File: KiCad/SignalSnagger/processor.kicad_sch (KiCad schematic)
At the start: 84 parts, among them J201 Conn_01x01_Female, J202 Conn_01x01_Female, J203 Conn_01x02, J204 Conn_01x02, J205 Conn_01x01_Female, J206 Conn_01x01_Female, J207 Conn_01x01_Female, J210 Conn_01x01_Female, J211 Conn_01x01_Female, J212 Conn_01x01_Female, J213 Conn_01x01_Female, J214 Conn_01x01_Female, J215 Conn_01x01_Female, J216 Conn_01x01_Female, J217 Conn_01x01_Female, J218 Conn_01x02, J219 Conn_01x02, J220 Conn_01x02, J221 Conn_01x02, P201 ISP/PDI, Q201 BSS84W-7-F, Q202 BSS138W-7-F, SW201 SW_SPST, SW202 SW_SPST, SW203 PEC12R-4225F-S0024, SW204 SW_SPST, SW205 SW_SPST, U201 AVR128DA48, U202 SI5351, U203 LP2985-5.0, U204 LP2985-3.3, U205 EA_DOGS104W-A, U206 LP2985-5.0, U207 MAX1683EUK, X202 25 MHz, X901 ECS-327TXO-30-TR

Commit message: Ver 0.317
PCB Tweaks
FreeCAD model updates
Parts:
- X901: value ECS-327TXO-30-TR -> (none); footprint Oscillator:Oscillator_SMD_ECS_327TXO -> (none)
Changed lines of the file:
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@@
   (title_block
     (title "SignalSnagger")
-    (date "2024-04-11")
-    (rev "0.316")
+    (date "2024-04-13")
+    (rev "0.317")
   )
   (bus_alias "PROC_BUS" (members "PA7" "PA6" "PA5" "PA4" "PA3" "PA2" "PA1" "PA0" "PB5" "PB4" "SCL1" "SDA1" "PB1" "PB0" "PC7" "PC6" "PC5" "PC4" "SCL0" "SDA0" "RXD1" "TXD1" "ADC7" "DAC0" "ADC5" "ADC4" "ADC3" "ADC2" "ADC1" "ADC0" "PE3" "PE2" "RXD4" "TXD4" "PF6" "PF5" "PF4" "PF3" "PF2"))
@@
     (in_bom yes) (on_board yes)
     (property "Reference" "X901" (id 0) (at 26.67 106.68 90))
-    (property "Value" "ECS-327TXO-30-TR" (id 1) (at 32.0985 105.5362 0)
+    (property "Value" "" (id 1) (at 32.0985 105.5362 0)
       (effects (font (size 1.27 1.27)) hide)
     )
-    (property "Footprint" "Oscillator:Oscillator_SMD_ECS_327TXO" (id 2) (at 52.07 114.3 0)
+    (property "Footprint" "" (id 2) (at 52.07 114.3 0)
       (effects (font (size 1.27 1.27)) hide)
     )

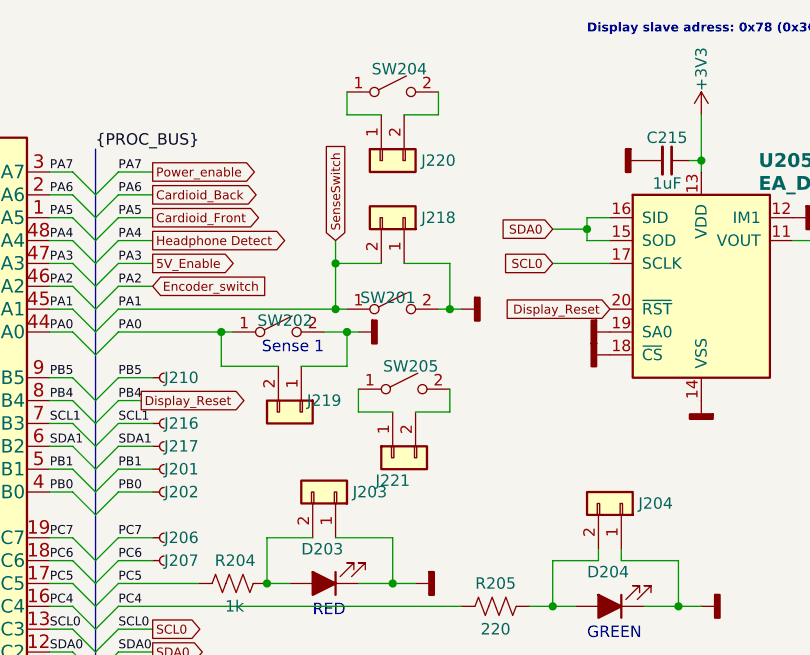
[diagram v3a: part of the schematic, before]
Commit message: Removed spare sense switches
Updated schematic and PCB to remove spare sense switches.
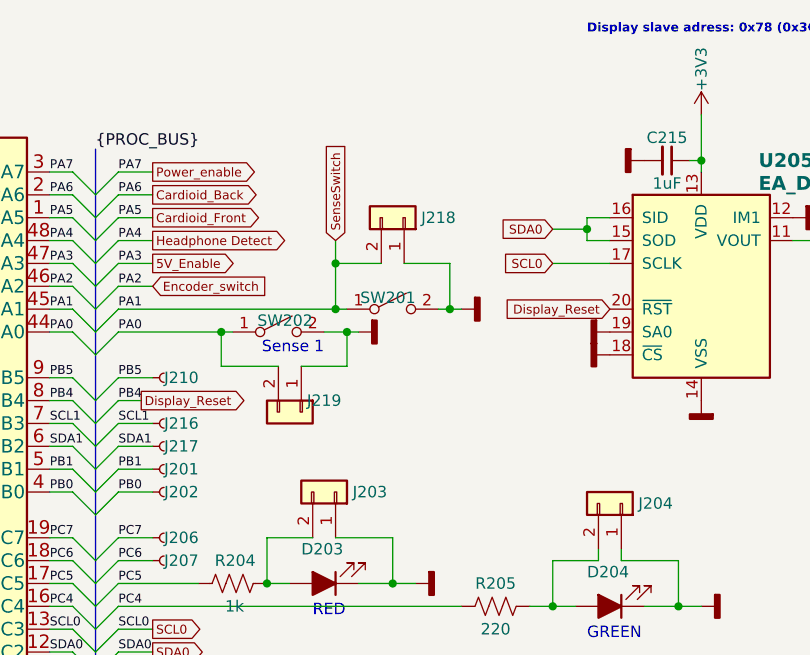
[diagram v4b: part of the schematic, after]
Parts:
- removed J220, J221: Conn_01x02, Connector_PinSocket_1.27mm:PinSocket_1x02_P1.27mm_Vertical, symbol Connector_Generic:Conn_01x02
- removed SW204, SW205: SW_SPST, Button_Switch_SMD:SW_SPST_TL1014BF160QG, symbol Switch:SW_SPST
- X901: value (none) -> ECS-327TXO-30-TR; footprint (none) -> Oscillator:Oscillator_SMD_ECS_327TXO
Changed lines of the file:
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@@
     (stroke (width 0) (type default) (color 0 0 0 0))
   )
-  (wire (pts (xy 129.54 67.31) (xy 125.73 67.31))
-    (stroke (width 0) (type default) (color 0 0 0 0))
-  )
   (wire (pts (xy 99.06 45.72) (xy 102.87 45.72))
     (stroke (width 0) (type default) (color 0 0 0 0))
@@
     (stroke (width 0) (type default) (color 0 0 0 0))
   )
-  (wire (pts (xy 130.81 34.29) (xy 134.62 34.29))
-    (stroke (width 0) (type default) (color 0 0 0 0))
-  )
   (wire (pts (xy 154.94 184.15) (xy 154.94 182.88))
     (stroke (width 0) (type default) (color 0 0 0 0))
@@
     (stroke (width 0) (type default) (color 0 0 0 0))
   )
-  (wire (pts (xy 132.08 67.31) (xy 135.89 67.31))
-    (stroke (width 0) (type default) (color 0 0 0 0))
-  )
   (wire (pts (xy 99.06 66.04) (xy 101.6 66.04))
     (stroke (width 0) (type default) (color 0 0 0 0))
@@
     (stroke (width 0) (type default) (color 0 0 0 0))
   )
-  (wire (pts (xy 128.27 34.29) (xy 124.46 34.29))
-    (stroke (width 0) (type default) (color 0 0 0 0))
-  )
   (wire (pts (xy 220.98 153.67) (xy 227.33 153.67))
     (stroke (width 0) (type default) (color 0 0 0 0))
@@
     (stroke (width 0) (type default) (color 0 0 0 0))
   )
-  (wire (pts (xy 124.46 34.29) (xy 124.46 31.75))
-    (stroke (width 0) (type default) (color 0 0 0 0))
-  )
   (bus (pts (xy 96.52 132.08) (xy 96.52 134.62))
     (stroke (width 0) (type default) (color 0 0 0 0))
@@
     (stroke (width 0) (type default) (color 0 0 0 0))
   )
-  (wire (pts (xy 134.62 34.29) (xy 134.62 31.75))
-    (stroke (width 0) (type default) (color 0 0 0 0))
-  )
   (wire (pts (xy 154.94 182.88) (xy 151.13 182.88))
     (stroke (width 0) (type default) (color 0 0 0 0))
@@
     (stroke (width 0) (type default) (color 0 0 0 0))
   )
-  (wire (pts (xy 125.73 67.31) (xy 125.73 64.77))
-    (stroke (width 0) (type default) (color 0 0 0 0))
-  )
   (wire (pts (xy 144.78 88.9) (xy 147.32 88.9))
     (stroke (width 0) (type default) (color 0 0 0 0))
@@
     (stroke (width 0) (type default) (color 0 0 0 0))
   )
-  (wire (pts (xy 135.89 67.31) (xy 135.89 64.77))
-    (stroke (width 0) (type default) (color 0 0 0 0))
-  )
   (wire (pts (xy 99.06 127) (xy 102.87 127))
     (stroke (width 0) (type default) (color 0 0 0 0))
@@
     (pin "1")
   )
-  (symbol (lib_id "Switch:SW_SPST") (at 130.81 64.77 0) (unit 1)
-    (in_bom yes) (on_board yes)
-    (property "Reference" "SW205" (id 0) (at 134.62 62.23 0)
-      (effects (font (size 1.27 1.27)) (justify right))
-    )
-    (property "Value" "SW_SPST" (id 1) (at 132.5122 65.913 90)
-      (effects (font (size 1.27 1.27)) (justify right) hide)
-    )
-    (property "Footprint" "Button_Switch_SMD:SW_SPST_TL1014BF160QG" (id 2) (at 130.81 64.77 0)
-      (effects (font (size 1.27 1.27)) hide)
-    )
-    (property "Datasheet" "~" (id 3) (at 130.81 64.77 0)
-      (effects (font (size 1.27 1.27)) hide)
-    )
-    (property "Digi-Key Part No." "N/P" (id 4) (at 130.81 64.77 0)
-      (effects (font (size 1.27 1.27)) hide)
-    )
-    (property "Manufacturer" "E-Switch" (id 5) (at 130.81 64.77 0)
-      (effects (font (size 1.27 1.27)) hide)
-    )
-    (property "Manufacturer PN" "TL1014BF160QG" (id 6) (at 130.81 64.77 0)
-      (effects (font (size 1.27 1.27)) hide)
-    )
-    (property "Description" "SWITCH TACTILE SPST-NO 0.05A 12V" (id 7) (at 130.81 64.77 0)
-      (effects (font (size 1.27 1.27)) hide)
-    )
-    (property "Link" "https://www.digikey.com/en/products/detail/e-switch/TL1014BF160QG/3910805" (id 8) (at 130.81 64.77 0)
-      (effects (font (size 1.27 1.27)) hide)
-    )
-    (pin "1")
-    (pin "2")
-  )
   (symbol (lib_id "Connector_Generic:Conn_02x03_Odd_Even") (at 33.02 157.48 0) (mirror y) (unit 1)
     (in_bom yes) (on_board yes) (fields_autoplaced)
@@
     (pin "2")
   )
-  (symbol (lib_id "Switch:SW_SPST") (at 129.54 31.75 0) (unit 1)
-    (in_bom yes) (on_board yes)
-    (property "Reference" "SW204" (id 0) (at 133.35 29.21 0)
-      (effects (font (size 1.27 1.27)) (justify right))
-    )
-    (property "Value" "SW_SPST" (id 1) (at 131.2422 32.893 90)
-      (effects (font (size 1.27 1.27)) (justify right) hide)
-    )
-    (property "Footprint" "Button_Switch_SMD:SW_SPST_TL1014BF160QG" (id 2) (at 129.54 31.75 0)
-      (effects (font (size 1.27 1.27)) hide)
-    )
-    (property "Datasheet" "~" (id 3) (at 129.54 31.75 0)
-      (effects (font (size 1.27 1.27)) hide)
-    )
-    (property "Digi-Key Part No." "N/P" (id 4) (at 129.54 31.75 0)
-      (effects (font (size 1.27 1.27)) hide)
-    )
-    (property "Manufacturer" "E-Switch" (id 5) (at 129.54 31.75 0)
-      (effects (font (size 1.27 1.27)) hide)
-    )
-    (property "Manufacturer PN" "TL1014BF160QG" (id 6) (at 129.54 31.75 0)
-      (effects (font (size 1.27 1.27)) hide)
-    )
-    (property "Description" "SWITCH TACTILE SPST-NO 0.05A 12V" (id 7) (at 129.54 31.75 0)
-      (effects (font (size 1.27 1.27)) hide)
-    )
-    (property "Link" "https://www.digikey.com/en/products/detail/e-switch/TL1014BF160QG/3910805" (id 8) (at 129.54 31.75 0)
-      (effects (font (size 1.27 1.27)) hide)
-    )
-    (pin "1")
-    (pin "2")
-  )
   (symbol (lib_id "power:GNDD") (at 153.67 58.42 270) (unit 1)
     (in_bom yes) (on_board yes)
@@
     (pin "1")
   )
-  (symbol (lib_id "Connector_Generic:Conn_01x02") (at 129.54 72.39 90) (mirror x) (unit 1)
-    (in_bom yes) (on_board yes)
-    (property "Reference" "J221" (id 0) (at 129.54 74.93 90))
-    (property "Value" "Conn_01x02" (id 1) (at 127.1071 72.39 0)
-      (effects (font (size 1.27 1.27)) hide)
-    )
-    (property "Footprint" "Connector_PinSocket_1.27mm:PinSocket_1x02_P1.27mm_Vertical" (id 2) (at 129.54 72.39 0)
-      (effects (font (size 1.27 1.27)) hide)
-    )
-    (property "Datasheet" "~" (id 3) (at 129.54 72.39 0)
-      (effects (font (size 1.27 1.27)) hide)
-    )
-    (property "Digi-Key Part No." "N/P" (id 4) (at 129.54 72.39 0)
-      (effects (font (size 1.27 1.27)) hide)
-    )
-    (pin "1")
-    (pin "2")
-  )
-  (symbol (lib_id "Connector_Generic:Conn_01x02") (at 128.27 39.37 90) (mirror x) (unit 1)
-    (in_bom yes) (on_board yes)
-    (property "Reference" "J220" (id 0) (at 134.62 39.37 90))
-    (property "Value" "Conn_01x02" (id 1) (at 125.8371 39.37 0)
-      (effects (font (size 1.27 1.27)) hide)
-    )
-    (property "Footprint" "Connector_PinSocket_1.27mm:PinSocket_1x02_P1.27mm_Vertical" (id 2) (at 128.27 39.37 0)
-      (effects (font (size 1.27 1.27)) hide)
-    )
-    (property "Datasheet" "~" (id 3) (at 128.27 39.37 0)
-      (effects (font (size 1.27 1.27)) hide)
-    )
-    (property "Digi-Key Part No." "N/P" (id 4) (at 128.27 39.37 0)
-      (effects (font (size 1.27 1.27)) hide)
-    )
-    (pin "1")
-    (pin "2")
-  )
   (symbol (lib_id "Device:C_Small") (at 106.68 179.07 270) (unit 1)
     (in_bom yes) (on_board yes)
@@
     (in_bom yes) (on_board yes)
     (property "Reference" "X901" (id 0) (at 26.67 106.68 90))
-    (property "Value" "" (id 1) (at 32.0985 105.5362 0)
+    (property "Value" "ECS-327TXO-30-TR" (id 1) (at 32.0985 105.5362 0)
       (effects (font (size 1.27 1.27)) hide)
     )
-    (property "Footprint" "" (id 2) (at 52.07 114.3 0)
+    (property "Footprint" "Oscillator:Oscillator_SMD_ECS_327TXO" (id 2) (at 52.07 114.3 0)
       (effects (font (size 1.27 1.27)) hide)
     )

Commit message: BOM Updates
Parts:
- U203: value LP2985-5.0 -> (none); footprint Package_TO_SOT_SMD:SOT-23-5 -> (none); LCSC Part Number C89826 -> (none); Link https://www.digikey.com/short/vr2m3rjp -> https://www.digikey.com/short/pr7whwn5
- U204: value LP2985-3.3 -> (none); footprint Package_TO_SOT_SMD:SOT-23-5 -> (none); Digi-Key Part No. 296-20717-1-ND -> 296-18476-1-ND; LCSC Part Number C89826 -> (none); Link https://www.digikey.com/short/vr2m3rjp -> https://www.digikey.com/en/products/detail/texas-instrument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; Manufacturer PN LP2985-50DBVR -> LP2985-33DBVR
- U205: value EA_DOGS104W-A -> (none); footprint Display:EA_DOGS104X-A -> (none)
- U206: LCSC Part Number C89826 -> (none); Link https://www.digikey.com/short/vr2m3rjp -> https://www.digikey.com/short/pr7whwn5
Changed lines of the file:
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@@
   (junction (at 220.98 97.79) (diameter 0) (color 0 0 0 0)
   )
-  (junction (at 168.91 152.4) (diameter 0) (color 0 0 0 0)
-  )
   (junction (at 125.73 106.68) (diameter 0) (color 0 0 0 0)
   )
@@
   (junction (at 223.52 95.25) (diameter 0) (color 0 0 0 0)
   )
+  (junction (at 168.91 152.4) (diameter 0) (color 0 0 0 0)
+  )
   (junction (at 147.32 88.9) (diameter 0) (color 0 0 0 0)
   )
@@
       (effects (font (size 1.54 1.54) bold) (justify left))
     )
-    (property "Value" "EA_DOGS104W-A" (id 1) (at 170.18 41.91 0)
+    (property "Value" "" (id 1) (at 170.18 41.91 0)
       (effects (font (size 1.54 1.54) bold) (justify left))
     )
-    (property "Footprint" "Display:EA_DOGS104X-A" (id 2) (at 163.83 68.58 0)
+    (property "Footprint" "" (id 2) (at 163.83 68.58 0)
       (effects (font (size 1.27 1.27)) hide)
     )
@@
       (effects (font (size 1.54 1.54) bold))
     )
-    (property "Value" "LP2985-5.0" (id 1) (at 142.24 176.53 0)
+    (property "Value" "" (id 1) (at 142.24 176.53 0)
       (effects (font (size 1.54 1.54) bold))
     )
-    (property "Footprint" "Package_TO_SOT_SMD:SOT-23-5" (id 2) (at 140.97 174.625 0)
+    (property "Footprint" "" (id 2) (at 140.97 174.625 0)
       (effects (font (size 1.27 1.27)) hide)
     )
@@
       (effects (font (size 1.27 1.27)) hide)
     )
-    (property "Description" "IC REG LINEAR 3.3V 150MA SOT23-5" (id 7) (at 140.97 182.88 0)
-      (effects (font (size 1.27 1.27)) hide)
-    )
-    (property "Link" "https://www.digikey.com/short/vr2m3rjp" (id 8) (at 140.97 182.88 0)
+    (property "Description" "IC REG LINEAR 5.0V 150MA SOT23-5" (id 7) (at 140.97 182.88 0)
       (effects (font (size 1.27 1.27)) hide)
     )
-    (property "LCSC Part Number" "C89826" (id 9) (at 140.97 182.88 0)
+    (property "Link" "https://www.digikey.com/short/pr7whwn5" (id 8) (at 140.97 182.88 0)
       (effects (font (size 1.27 1.27)) hide)
     )
@@
     (pin "2")
   )
+  (symbol (lib_id "Regulator_Linear:LP2985-3.3") (at 179.07 154.94 0) (unit 1)
+    (in_bom yes) (on_board yes)
+    (property "Reference" "U206" (id 0) (at 179.07 144.78 0)
+      (effects (font (size 1.54 1.54) bold))
+    )
+    (property "Value" "LP2985-5.0" (id 1) (at 180.34 148.59 0)
+      (effects (font (size 1.54 1.54) bold))
+    )
+    (property "Footprint" "Package_TO_SOT_SMD:SOT-23-5" (id 2) (at 179.07 146.685 0)
+      (effects (font (size 1.27 1.27)) hide)
+    )
+    (property "Datasheet" "" (id 3) (at 179.07 154.94 0)
+      (effects (font (size 1.27 1.27)) hide)
+    )
+    (property "Digi-Key Part No." "296-20717-1-ND" (id 4) (at 179.07 154.94 0)
+      (effects (font (size 1.27 1.27)) hide)
+    )
+    (property "Manufacturer" "Texas Instruments" (id 5) (at 179.07 154.94 0)
+      (effects (font (size 1.27 1.27)) hide)
+    )
+    (property "Manufacturer PN" "LP2985-50DBVR" (id 6) (at 179.07 154.94 0)
+      (effects (font (size 1.27 1.27)) hide)
+    )
+    (property "Description" "IC REG LINEAR 5.0V 150MA SOT23-5" (id 7) (at 179.07 154.94 0)
+      (effects (font (size 1.27 1.27)) hide)
+    )
+    (property "Link" "https://www.digikey.com/short/pr7whwn5" (id 8) (at 179.07 154.94 0)
+      (effects (font (size 1.27 1.27)) hide)
+    )
+    (pin "1")
+    (pin "2")
+    (pin "3")
+    (pin "4")
+    (pin "5")
+  )
   (symbol (lib_id "power:GND") (at 161.29 152.4 270) (unit 1)
     (in_bom yes) (on_board yes) (fields_autoplaced)
@@
       (effects (font (size 1.54 1.54) bold))
     )
-    (property "Value" "LP2985-3.3" (id 1) (at 78.74 189.23 0)
+    (property "Value" "" (id 1) (at 78.74 189.23 0)
       (effects (font (size 1.54 1.54) bold))
     )
-    (property "Footprint" "Package_TO_SOT_SMD:SOT-23-5" (id 2) (at 90.17 173.355 0)
+    (property "Footprint" "" (id 2) (at 90.17 173.355 0)
       (effects (font (size 1.27 1.27)) hide)
     )
@@
       (effects (font (size 1.27 1.27)) hide)
     )
-    (property "Digi-Key Part No." "296-20717-1-ND" (id 4) (at 90.17 181.61 0)
+    (property "Digi-Key Part No." "296-18476-1-ND" (id 4) (at 90.17 181.61 0)
       (effects (font (size 1.27 1.27)) hide)
     )
@@
       (effects (font (size 1.27 1.27)) hide)
     )
-    (property "Manufacturer PN" "LP2985-50DBVR" (id 6) (at 90.17 181.61 0)
+    (property "Manufacturer PN" "LP2985-33DBVR" (id 6) (at 90.17 181.61 0)
       (effects (font (size 1.27 1.27)) hide)
     )
@@
       (effects (font (size 1.27 1.27)) hide)
     )
-    (property "Link" "https://www.digikey.com/short/vr2m3rjp" (id 8) (at 90.17 181.61 0)
-      (effects (font (size 1.27 1.27)) hide)
-    )
-    (property "LCSC Part Number" "C89826" (id 9) (at 90.17 181.61 0)
+    (property "Link" "https://www.digikey.com/en/products/detail/texas-instruments/LP2985-33DBVR/809759" (id 8) (at 90.17 181.61 0)
       (effects (font (size 1.27 1.27)) hide)
     )
@@
     (pin "1")
   )
-  (symbol (lib_id "Regulator_Linear:LP2985-3.3") (at 179.07 154.94 0) (unit 1)
-    (in_bom yes) (on_board yes)
-    (property "Reference" "U206" (id 0) (at 179.07 146.05 0)
-      (effects (font (size 1.54 1.54) bold))
-    )
-    (property "Value" "LP2985-5.0" (id 1) (at 180.34 148.59 0)
-      (effects (font (size 1.54 1.54) bold))
-    )
-    (property "Footprint" "Package_TO_SOT_SMD:SOT-23-5" (id 2) (at 179.07 146.685 0)
-      (effects (font (size 1.27 1.27)) hide)
-    )
-    (property "Datasheet" "" (id 3) (at 179.07 154.94 0)
-      (effects (font (size 1.27 1.27)) hide)
-    )
-    (property "Digi-Key Part No." "296-20717-1-ND" (id 4) (at 179.07 154.94 0)
-      (effects (font (size 1.27 1.27)) hide)
-    )
-    (property "Manufacturer" "Texas Instruments" (id 5) (at 179.07 154.94 0)
-      (effects (font (size 1.27 1.27)) hide)
-    )
-    (property "Manufacturer PN" "LP2985-50DBVR" (id 6) (at 179.07 154.94 0)
-      (effects (font (size 1.27 1.27)) hide)
-    )
-    (property "Description" "IC REG LINEAR 3.3V 150MA SOT23-5" (id 7) (at 179.07 154.94 0)
-      (effects (font (size 1.27 1.27)) hide)
-    )
-    (property "Link" "https://www.digikey.com/short/vr2m3rjp" (id 8) (at 179.07 154.94 0)
-      (effects (font (size 1.27 1.27)) hide)
-    )
-    (property "LCSC Part Number" "C89826" (id 9) (at 179.07 154.94 0)
-      (effects (font (size 1.27 1.27)) hide)
-    )
-    (pin "1")
-    (pin "2")
-    (pin "3")
-    (pin "4")
-    (pin "5")
-  )
   (symbol (lib_id "power:GNDD") (at 17.78 66.04 270) (unit 1)
